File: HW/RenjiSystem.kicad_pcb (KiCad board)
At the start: 2 copper layers, 45 parts, among them J1 Conn_AE_LXDC55_3.3V, J10 Conn_Debug, J11 Conn_AE_QFP100PR5_DIP_51_75, J12 Conn_SwitchBoard, J13 Conn_LEDIndicator, J2 Conn_LCD, J3 Conn_AE_QFP100PR5_DIP_26_50, J4 Conn_AE_QFP100PR5_DIP_1_25, J5 Conn_AE_LXDC55_5V, J6 Conn_AE_QFP100PR5_DIP_76_100, J7 Conn_Ethernet, J8 Conn_UART1, J9 Conn_UART2, K1 G5Q-14_DC5, K2 G5Q-14_DC5, K3 G5Q-14_DC5, Q1 2SC1815, Q2 2SC1815, Q3 2SC1815, T1 Transformer_FS24-100-C2

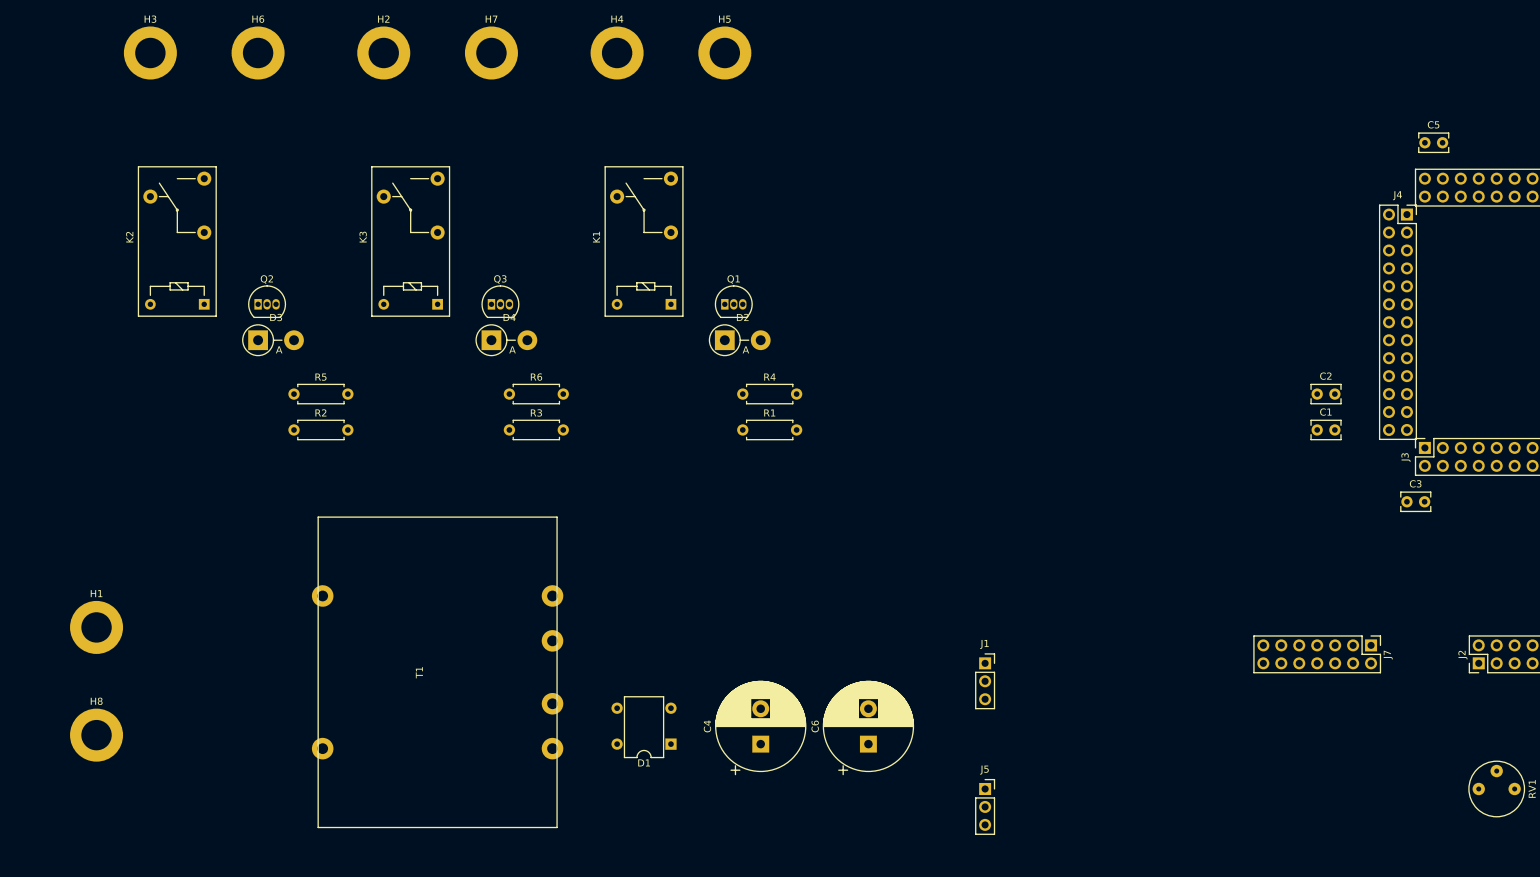
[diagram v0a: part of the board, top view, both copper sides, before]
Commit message: 電源部配線
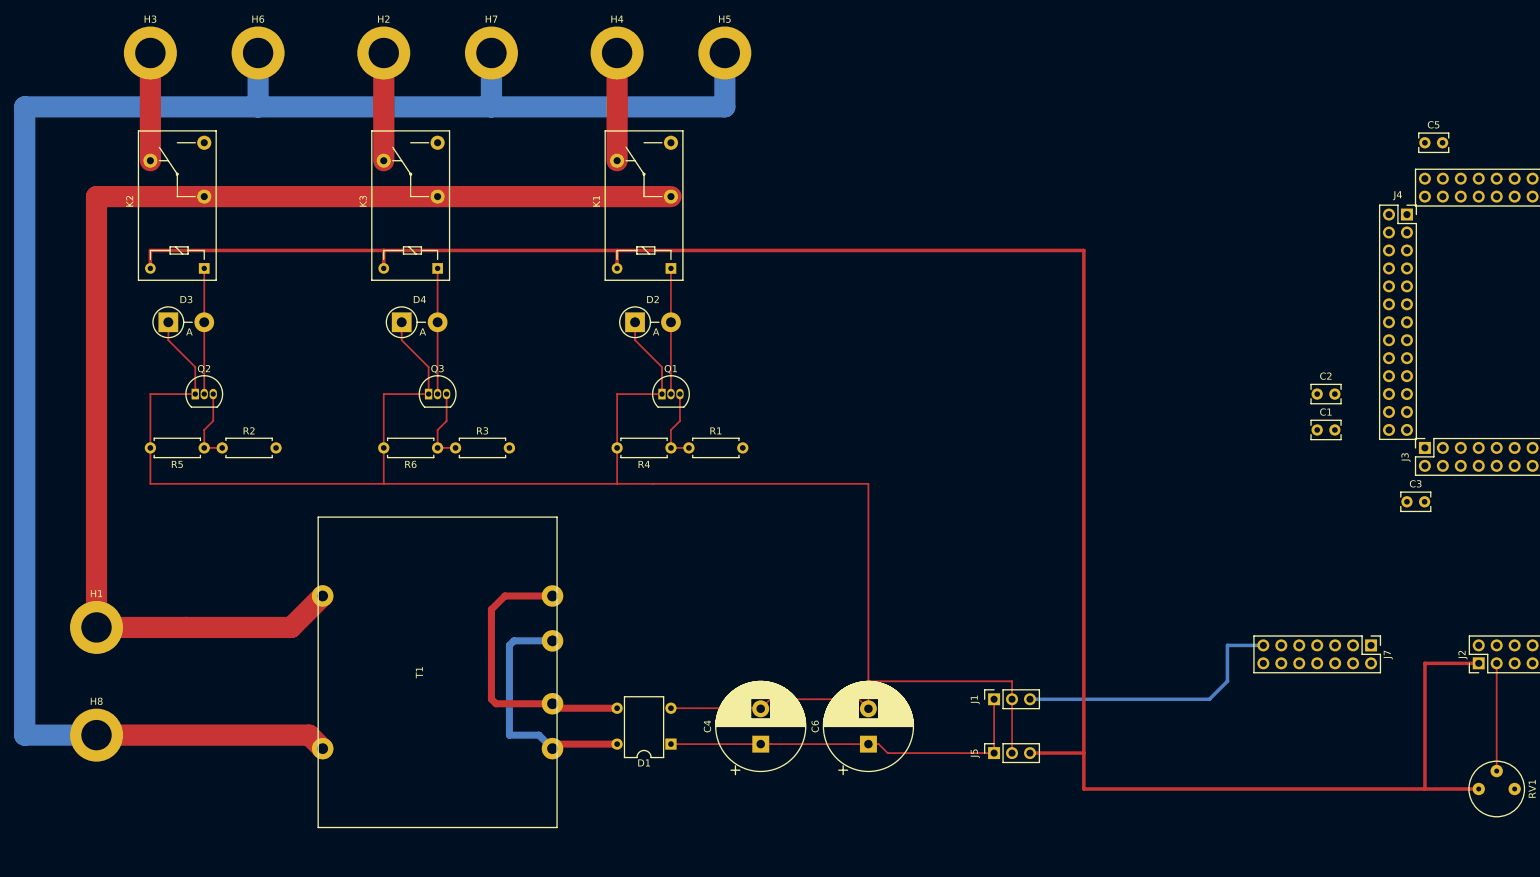
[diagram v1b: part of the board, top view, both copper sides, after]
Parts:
- moved Q1 15.5 mm to (105.4, 66.0)
- moved Q2 15.5 mm to (39.4, 66.0)
- moved Q3 15.5 mm to (72.4, 66.0)
- moved R5 14.8 mm to (40.6, 73.7), turned to 180 degrees
- moved D2 13.0 mm to (101.6, 55.9)
- moved D4 13.0 mm to (68.6, 55.9)
- moved D3 13.0 mm to (35.6, 55.9)
- moved R4 12.7 mm to (106.7, 73.7), turned to 180 degrees
- moved R6 12.7 mm to (73.7, 73.7), turned to 180 degrees
- moved R2 10.5 mm to (43.2, 73.7)
- moved R1 8.03 mm to (109.2, 73.7)
- moved R3 8.03 mm to (76.2, 73.7)
- moved J1 5.24 mm to (152.4, 109.2), turned to 90 degrees
- moved J5 5.24 mm to (152.4, 116.8), turned to 90 degrees
- moved K1 5.08 mm to (106.7, 48.3)
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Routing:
- net +5V: track 0.00 -> 304.8 mm
- net GND: track 0.00 -> 285.4 mm
- net Earth: track 0.00 -> 253.8 mm
- net POWER_IN_HOT: track 0.00 -> 176.1 mm
- net +9V: track 0.00 -> 53.9 mm
- net Net-(D1-Pad3): track 0.00 -> 40.4 mm
- net +3V3: track 0.00 -> 39.2 mm
- net Net-(D1-Pad4): track 0.00 -> 35.4 mm
- net Net-(D4-Pad2): track 0.00 -> 17.8 mm
- net Net-(D3-Pad2): track 0.00 -> 17.8 mm
- net Net-(D2-Pad2): track 0.00 -> 17.8 mm
- net Net-(H4-Pad1): track 0.00 -> 15.2 mm
- net Net-(H3-Pad1): track 0.00 -> 15.2 mm
- net Net-(H2-Pad1): track 0.00 -> 15.2 mm
- net CONTRAST_ADJ: track 0.00 -> 15.2 mm
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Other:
- net class AC100VLine added: clearance 10, trace_width 3, via_dia 1.5, via_drill 1.1
- net class AC12VLine added: clearance 3, trace_width 1, via_dia 0.8, via_drill 0.4
- net class DC3.3VPowerLine added: clearance 0.5, trace_width 0.5, via_dia 0.8, via_drill 0.4
- net class DC5VPowerLine added: clearance 0.5, trace_width 0.5, via_dia 0.8, via_drill 0.4
- net class DC9VPowerLine added: clearance 1, trace_width 0.8, via_dia 0.8, via_drill 0.4

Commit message: ボード回路図を, シート分割
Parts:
- moved J9 116.9 mm to (274.3, 16.5), turned to 0 degrees
- moved J8 102.3 mm to (274.3, 27.9), turned to 0 degrees
- moved J10 87.8 mm to (274.3, 39.4), turned to 0 degrees
- moved J12 70.1 mm to (191.8, 34.3)
- moved Q2 50.8 mm to (90.2, 66.0)
- moved R2 50.8 mm to (94.0, 73.7)
- moved D3 50.8 mm to (86.4, 55.9)
- moved R5 50.8 mm to (91.4, 73.7)
- moved C5 41.9 mm to (254.0, 40.6)
- moved H2 33.0 mm to (33.0, 17.8)
- moved H3 33.0 mm to (66.0, 17.8)
- moved H6 33.0 mm to (81.3, 17.8)
- moved H7 33.0 mm to (48.3, 17.8)
- moved K2 33.0 mm to (73.7, 48.3)
- moved K3 33.0 mm to (40.6, 48.3)
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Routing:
- net +3V3: track 39.2 -> 295.4 mm, vias 0 -> 2
- net GND: track 285.4 -> 36.9 mm, vias 0 -> 1
- net FAN_CONTROL_SIGNAL: track 0.00 -> 193.6 mm, vias 0 -> 1
- net HEATER_CONTROL_SIGNAL: track 0.00 -> 160.6 mm, vias 0 -> 1
- net UV_CONTROL_SIGNAL: track 0.00 -> 122.5 mm, vias 0 -> 1
- net +5V: track 304.8 -> 383.5 mm
- net NRST: track 0.00 -> 68.7 mm
- net ETH_TXD1: track 0.00 -> 65.8 mm
- net ETH_TXD0: track 0.00 -> 65.8 mm
- net ETH_MDC: track 0.00 -> 60.2 mm
- net UART2_TX: track 0.00 -> 56.2 mm
- net ETH_TX_EN: track 0.00 -> 51.4 mm
- net UART2_RX: track 0.00 -> 50.0 mm
- net ETH_RXD1: track 0.00 -> 39.9 mm
- net UART1_RX: track 0.00 -> 39.9 mm
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- added copper zone on B.Cu, net GND
- added copper zone on F.Cu, net GND
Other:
- net class AC100VLine: clearance 10 -> 1.3; trace_width 3 -> 2
- net class AC12VLine: clearance 3 -> 0.65
- net class DC3.3VPowerLine: clearance 0.5 -> 0.25; trace_width 0.5 -> 0.25
- net class DC5VPowerLine: clearance 0.5 -> 0.25
- net class DC9VPowerLine: clearance 1 -> 0.25

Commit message: Ethernetボードの配置のためにレイアウト変更
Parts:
- removed H7: MountingHole_Pad_FAN_COLD, MountingHole:MountingHole_4.3mm_M4_DIN965_Pad
- removed H8: MountingHole_Pad_AC100V_COLD, MountingHole:MountingHole_4.3mm_M4_DIN965_Pad
- added J14: Conn_AE_QFP100PR5_DIP_76_100, Connector_PinSocket_2.54mm:PinSocket_2x13_P2.54mm_Vertical, F.Cu at (233.7, 91.4)
- added J15: Conn_LCD, Connector_PinHeader_2.54mm:PinHeader_2x07_P2.54mm_Vertical, F.Cu at (194.3, 41.9)
- added J16: Conn_Ethernet, Connector_PinHeader_2.54mm:PinHeader_2x07_P2.54mm_Vertical, F.Cu at (160.0, 36.8)
- added J17: Conn_UART1, Connector_PinHeader_2.54mm:PinHeader_1x03_P2.54mm_Horizontal, F.Cu at (217.2, 130.8)
- added J18: Conn_UART2, Connector_PinHeader_2.54mm:PinHeader_1x03_P2.54mm_Horizontal, F.Cu at (205.7, 130.8)
- added J19: Conn_Debug, Connector_PinHeader_2.54mm:PinHeader_1x05_P2.54mm_Horizontal, F.Cu at (233.7, 130.8)
- added J20: Conn_SwitchBoard, Connector_PinSocket_2.54mm:PinSocket_1x08_P2.54mm_Vertical, F.Cu at (218.4, 41.9)
- added J21: Conn_LEDIndicator, Connector_PinSocket_2.54mm:PinSocket_1x06_P2.54mm_Vertical, F.Cu at (238.8, 41.9)
- C1: value 1uF -> CP1; footprint Capacitor_THT:C_Rect_L4.0mm_W2.5mm_P2.50mm -> Capacitor_THT:CP_Radial_D12.5mm_P5.00mm
- C2: value 10nF -> CP1; footprint Capacitor_THT:C_Rect_L4.0mm_W2.5mm_P2.50mm -> Capacitor_THT:CP_Radial_D12.5mm_P5.00mm
- C3: value 2.2uF -> 1uF
- C4: value CP1 -> 10nF; footprint Capacitor_THT:CP_Radial_D12.5mm_P5.00mm -> Capacitor_THT:C_Rect_L4.0mm_W2.5mm_P2.50mm
- C6: value CP1 -> 2.2uF; footprint Capacitor_THT:CP_Radial_D12.5mm_P5.00mm -> Capacitor_THT:C_Rect_L4.0mm_W2.5mm_P2.50mm
- H1: value MountingHole_Pad_AC100V_HOT -> MountingHole; footprint MountingHole:MountingHole_4.3mm_M4_DIN965_Pad -> MountingHole:MountingHole_3.2mm_M3
- H2: value MountingHole_Pad_FAN_HOT -> MountingHole; footprint MountingHole:MountingHole_4.3mm_M4_DIN965_Pad -> MountingHole:MountingHole_3.2mm_M3
- H3: value MountingHole_Pad_HEATER_HOT -> MountingHole; footprint MountingHole:MountingHole_4.3mm_M4_DIN965_Pad -> MountingHole:MountingHole_3.2mm_M3
- H4: value MountingHole_Pad_UV_HOT -> MountingHole; footprint MountingHole:MountingHole_4.3mm_M4_DIN965_Pad -> MountingHole:MountingHole_3.2mm_M3
- H5: value MountingHole_Pad_UV_COLD -> MountingHole; footprint MountingHole:MountingHole_4.3mm_M4_DIN965_Pad -> MountingHole:MountingHole_3.2mm_M3
- H6: value MountingHole_Pad_HEATER_COLD -> MountingHole; footprint MountingHole:MountingHole_4.3mm_M4_DIN965_Pad -> MountingHole:MountingHole_3.2mm_M3
- J1: value Conn_AE_LXDC55_3.3V -> Screw_Terminal_AC100VHOT; footprint Connector_PinSocket_2.54mm:PinSocket_1x03_P2.54mm_Vertical -> MyFootPrintLibrary:PCB-20(632)F
- J10: value Conn_Debug -> Conn_AE_LXDC55_5V; footprint Connector_PinHeader_2.54mm:PinHeader_1x05_P2.54mm_Horizontal -> Connector_PinSocket_2.54mm:PinSocket_1x03_P2.54mm_Vertical
- J11: value Conn_AE_QFP100PR5_DIP_51_75 -> Conn_AE_QFP100PR5_DIP_1_25
- J12: value Conn_SwitchBoard -> Conn_AE_QFP100PR5_DIP_26_50; footprint Connector_PinSocket_2.54mm:PinSocket_1x08_P2.54mm_Vertical -> Connector_PinSocket_2.54mm:PinSocket_2x13_P2.54mm_Vertical
- J13: value Conn_LEDIndicator -> Conn_AE_QFP100PR5_DIP_51_75; footprint Connector_PinSocket_2.54mm:PinSocket_1x06_P2.54mm_Vertical -> Connector_PinSocket_2.54mm:PinSocket_2x13_P2.54mm_Vertical
- J2: value Conn_LCD -> Screw_Terminal_AC100VCOLD; footprint Connector_PinHeader_2.54mm:PinHeader_2x07_P2.54mm_Vertical -> MyFootPrintLibrary:PCB-20(632)F
- J3: value Conn_AE_QFP100PR5_DIP_26_50 -> Screw_Terminal_UV_HOT; footprint Connector_PinSocket_2.54mm:PinSocket_2x13_P2.54mm_Vertical -> MyFootPrintLibrary:PCB-20(632)F
- J4: value Conn_AE_QFP100PR5_DIP_1_25 -> Screw_Terminal_UV_COLD; footprint Connector_PinSocket_2.54mm:PinSocket_2x13_P2.54mm_Vertical -> MyFootPrintLibrary:PCB-20(632)F
- J5: value Conn_AE_LXDC55_5V -> Screw_Terminal_HEATER_HOT; footprint Connector_PinSocket_2.54mm:PinSocket_1x03_P2.54mm_Vertical -> MyFootPrintLibrary:PCB-20(632)F
- J6: value Conn_AE_QFP100PR5_DIP_76_100 -> Screw_Terminal_HEATER_COLD; footprint Connector_PinSocket_2.54mm:PinSocket_2x13_P2.54mm_Vertical -> MyFootPrintLibrary:PCB-20(632)F
- J7: value Conn_Ethernet -> Screw_Terminal_FAN_HOT; footprint Connector_PinHeader_2.54mm:PinHeader_2x07_P2.54mm_Vertical -> MyFootPrintLibrary:PCB-20(632)F
- J8: value Conn_UART1 -> Screw_Terminal_FAN_COLD; footprint Connector_PinHeader_2.54mm:PinHeader_1x03_P2.54mm_Horizontal -> MyFootPrintLibrary:PCB-20(632)F
- J9: value Conn_UART2 -> Conn_AE_LXDC55_3.3V; footprint Connector_PinHeader_2.54mm:PinHeader_1x03_P2.54mm_Horizontal -> Connector_PinSocket_2.54mm:PinSocket_1x03_P2.54mm_Vertical
- R3: value 1k -> 10k
- R5: value 10k -> 1k
- moved H2 207.3 mm to (240.0, 29.2)
- moved H4 185.6 mm to (240.0, 138.4)
- moved J9 179.7 mm to (134.6, 129.5), turned to 90 degrees
- moved J2 169.7 mm to (52.1, 120.7), turned to 180 degrees
- moved H6 156.5 mm to (185.4, 134.6)
- moved J10 151.9 mm to (134.6, 99.1), turned to 90 degrees
- moved J4 148.4 mm to (62.5, 38.2), turned to 90 degrees
- moved J6 148.3 mm to (95.5, 38.1)
- moved J8 146.1 mm to (128.5, 38.2), turned to 270 degrees
- moved J3 139.5 mm to (78.5, 38.2)
- moved H5 126.9 mm to (163.8, 134.6)
- moved H3 123.0 mm to (41.9, 138.4)
- moved J1 101.1 mm to (51.6, 100.5), turned to 180 degrees
- moved C4 99.6 mm to (205.7, 66.0), turned to 180 degrees
- moved C6 97.4 mm to (228.6, 90.2), turned to 180 degrees
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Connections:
- C1 pad 1: GND -> /Power/Rectified_DC9V
- C1 pad 2: +3V3 -> GND
- C2 pad 1: +3V3 -> /Power/Rectified_DC9V
- C3 pad 1: Net-(C3-Pad1) -> GND
- C3 pad 2: GND -> +BATT
- C4 pad 1: +9V -> +BATT
- C5 pad 1: Net-(C5-Pad1) -> /MCU/VCAP1
- C6 pad 1: +9V -> /MCU/VCAP2
- D1 pad 1: +9V -> /Power/Rectified_DC9V
- H1 pad 1: POWER_IN_HOT -> (no net)
- H2 pad 1: Net-(H2-Pad1) -> (no net)
- H3 pad 1: Net-(H3-Pad1) -> (no net)
- H4 pad 1: Net-(H4-Pad1) -> (no net)
- H5 pad 1: Earth -> (no net)
- H6 pad 1: Earth -> (no net)
- J1 pad 1: +9V -> /Instruments/AC100V_HOT
- J10 pad 1: +3V3 -> /Power/Rectified_DC9V
- J10 pad 2: SYS_SWCLK -> GND
- J10 pad 3: GND -> /Instruments/CTRL_POWER_IN
- J11 pad 1: ETH_TXD0 -> /MCU/SETTING_BUTTON_UP
- J11 pad 10: Net-(J11-Pad10) -> GND
- J11 pad 11: UV_CONTROL_SIGNAL -> +BATT
- J11 pad 12: HEATER_CONTROL_SIGNAL -> (no net)
- J11 pad 13: FAN_CONTROL_SIGNAL -> (no net)
- J11 pad 14: Net-(J11-Pad14) -> /Debug/DBG2
- J11 pad 15: Net-(J11-Pad15) -> (no net)
- J11 pad 16: Net-(J11-Pad16) -> /Ethernet/ETHER_CTRL8
- J11 pad 17: Net-(J11-Pad17) -> (no net)
- J11 pad 18: UART1_TX -> (no net)
- J11 pad 19: UART1_RX -> +BATT
- J11 pad 2: ETH_TXD1 -> /MCU/SETTING_BUTTON_SELECT
- J11 pad 20: Net-(J11-Pad20) -> GND
- J11 pad 21: Net-(J11-Pad21) -> +BATT
- J11 pad 22: SYS_SWDIO -> +BATT
- J11 pad 23: Net-(C5-Pad1) -> (no net)
- J11 pad 24: GND -> /Ethernet/ETHER_CTRL3
- J11 pad 25: +3V3 -> /Ethernet/ETHER_CTRL4
- J11 pad 26: Net-(J11-Pad26) -> (no net)
- J11 pad 3: LED_SIGNAL_RED -> /MCU/SETTING_BUTTON_DOWN
- J11 pad 4: LED_SIGNAL_GREEN -> /MCU/SWITCH_SIGNAL3
- J11 pad 5: LED_SIGNAL_ORANGE -> /MCU/SWITCH_SIGNAL4
- J11 pad 6: LED_SIGNAL_GREEN2 -> +BATT
- J11 pad 7: Net-(J11-Pad7) -> /MCU/RESERVED_SWITCH1
- J11 pad 8: Net-(J11-Pad8) -> /MCU/RESERVED_SWITCH2
- J11 pad 9: Net-(J11-Pad9) -> (no net)
- J12 pad 1: SETTING_BUTTON_UP -> (no net)
- J12 pad 2: SETTING_BUTTON_SELECT -> GND
- J12 pad 3: SETTING_BUTTON_DOWN -> +BATT
- J12 pad 4: UV_CONTROL_SWTICH -> (no net)
- J12 pad 5: TEMP_SETTING_SWITCH -> (no net)
- J12 pad 6: RESERVED_SWITCH1 -> (no net)
- J12 pad 7: RESERVED_SWITCH2 -> /Ethernet/ETHER_CTRL7
- J12 pad 8: GND -> /Ethernet/ETHER_CTRL2
- J13 pad 1: +5V -> /Ethernet/ETHER_CTRL5
- J13 pad 2: LED_SIGNAL_RED -> /Ethernet/ETHER_CTRL0
- J13 pad 3: LED_SIGNAL_GREEN -> (no net)
- J13 pad 4: LED_SIGNAL_ORANGE -> (no net)
- J13 pad 5: LED_SIGNAL_GREEN2 -> (no net)
- J13 pad 6: GND -> (no net)
- J2 pad 1: +5V -> Earth
- J3 pad 1: Net-(J3-Pad1) -> /Instruments/UV_DRIVE_HOT
- J4 pad 1: SETTING_BUTTON_UP -> Earth
- J5 pad 1: +9V -> /Instruments/HEATER_DRIVE_HOT
- J6 pad 1: SYS_SWCLK -> Earth
- J7 pad 1: ETH_TXD1 -> /Instruments/FAN_DRIVE_HOT
- J8 pad 1: UART1_TX -> Earth
- J9 pad 1: UART2_TX -> /Power/Rectified_DC9V
- J9 pad 2: UART2_RX -> GND
- J9 pad 3: GND -> +BATT
- K1 pad 2: POWER_IN_HOT -> /Instruments/AC100V_HOT
- K1 pad 3: Net-(K1-Pad3) -> /Instruments/UV_DRIVE_HOT
- K1 pad 4: Net-(H4-Pad1) -> (no net)
- K1 pad 5: +5V -> /Instruments/CTRL_POWER_IN
- K2 pad 2: POWER_IN_HOT -> /Instruments/AC100V_HOT
- K2 pad 3: Net-(K2-Pad3) -> /Instruments/FAN_DRIVE_HOT
- K2 pad 4: Net-(H3-Pad1) -> (no net)
- K2 pad 5: +5V -> /Instruments/CTRL_POWER_IN
- K3 pad 2: POWER_IN_HOT -> /Instruments/AC100V_HOT
- K3 pad 3: Net-(K3-Pad3) -> /Instruments/HEATER_DRIVE_HOT
- K3 pad 4: Net-(H2-Pad1) -> (no net)
- K3 pad 5: +5V -> /Instruments/CTRL_POWER_IN
- R1 pad 2: UV_CONTROL_SIGNAL -> /MCU/HEATER_CONTROL_SIGNAL
- R2 pad 2: HEATER_CONTROL_SIGNAL -> /Instruments/FAN_CONTROL_SIGNAL
- R3 pad 1: Net-(Q3-Pad3) -> Net-(Q1-Pad3)
- R3 pad 2: FAN_CONTROL_SIGNAL -> GND
- R4 pad 1: Net-(Q1-Pad3) -> Net-(Q2-Pad3)
- R5 pad 1: Net-(Q2-Pad3) -> Net-(Q3-Pad3)
- R5 pad 2: GND -> /Instruments/HEATER_CONTROL_SIGNAL
- RV1 pad 1: +5V -> /Instruments/CTRL_POWER_IN
- RV1 pad 2: CONTRAST_ADJ -> /LCD/CONTRAST_ADJ
- T1 pad 1: POWER_IN_HOT -> /Instruments/AC100V_HOT
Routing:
- net +5V: track 383.5 -> 0.00 mm
- net +BATT: track 0.00 -> 346.2 mm
- net /Instruments/CTRL_POWER_IN: track 0.00 -> 296.5 mm
- net +3V3: track 295.4 -> 0.00 mm, vias 2 -> 0
- net FAN_CONTROL_SIGNAL: track 193.6 -> 0.00 mm, vias 1 -> 0
- net POWER_IN_HOT: track 176.1 -> 0.00 mm
- net /MCU/HEATER_CONTROL_SIGNAL: track 0.00 -> 171.4 mm
- net HEATER_CONTROL_SIGNAL: track 160.6 -> 0.00 mm, vias 1 -> 0
- net /Instruments/AC100V_HOT: track 0.00 -> 158.2 mm
- net /Instruments/HEATER_CONTROL_SIGNAL: track 0.00 -> 137.6 mm
- net UV_CONTROL_SIGNAL: track 122.5 -> 0.00 mm, vias 1 -> 0
- net /Instruments/FAN_CONTROL_SIGNAL: track 0.00 -> 104.6 mm
- net /Debug/UART21: track 0.00 -> 102.9 mm
- net /Ethernet/ETHER_CTRL5: track 0.00 -> 101.3 mm
- net /Ethernet/ETHER_CTRL0: track 0.00 -> 100.4 mm
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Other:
- board outline added: 205.7 x 116.8 mm
- net class AC100VLine: via_dia 1.5 -> 3.3; via_drill 1.1 -> 1.3
- net class AC12VLine removed
- net class DC3.3VPowerLine removed
- net class DC5VPowerLine removed
- net class DC9VPowerLine removed
- net class Default: trace_width 0.25 -> 0.4; via_dia 0.8 -> 1
- rule pad_to_mask_clearance: 0.051 -> 0
- board text added: "AE_LXDC55-3.3V"
- board text added: "AE_LXDC55-5V"
- board text added: "Ethernet"
- board text added: "LAN8720A board"
- board text added: "LCD"
- board text added: "LED board"
- board text added: "Switch board"

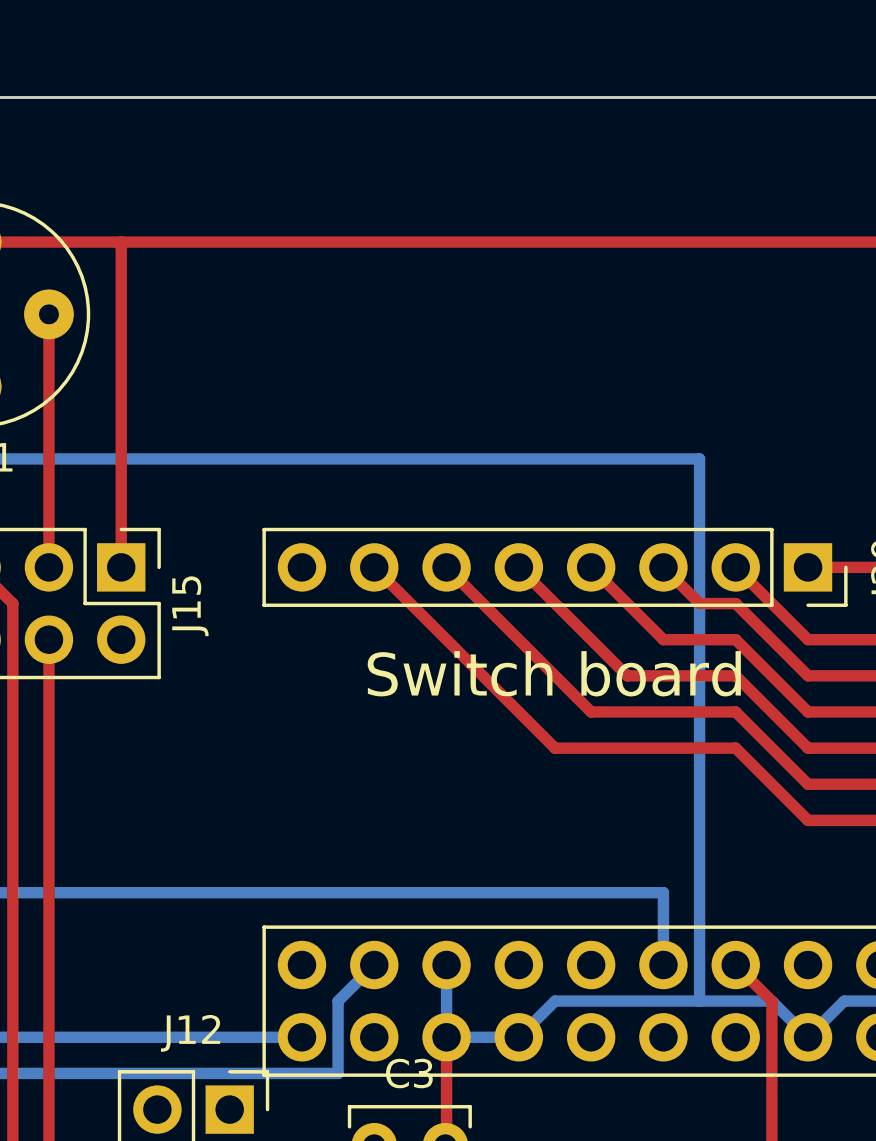
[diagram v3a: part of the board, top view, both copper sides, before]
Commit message: サーミスタの端子を追記
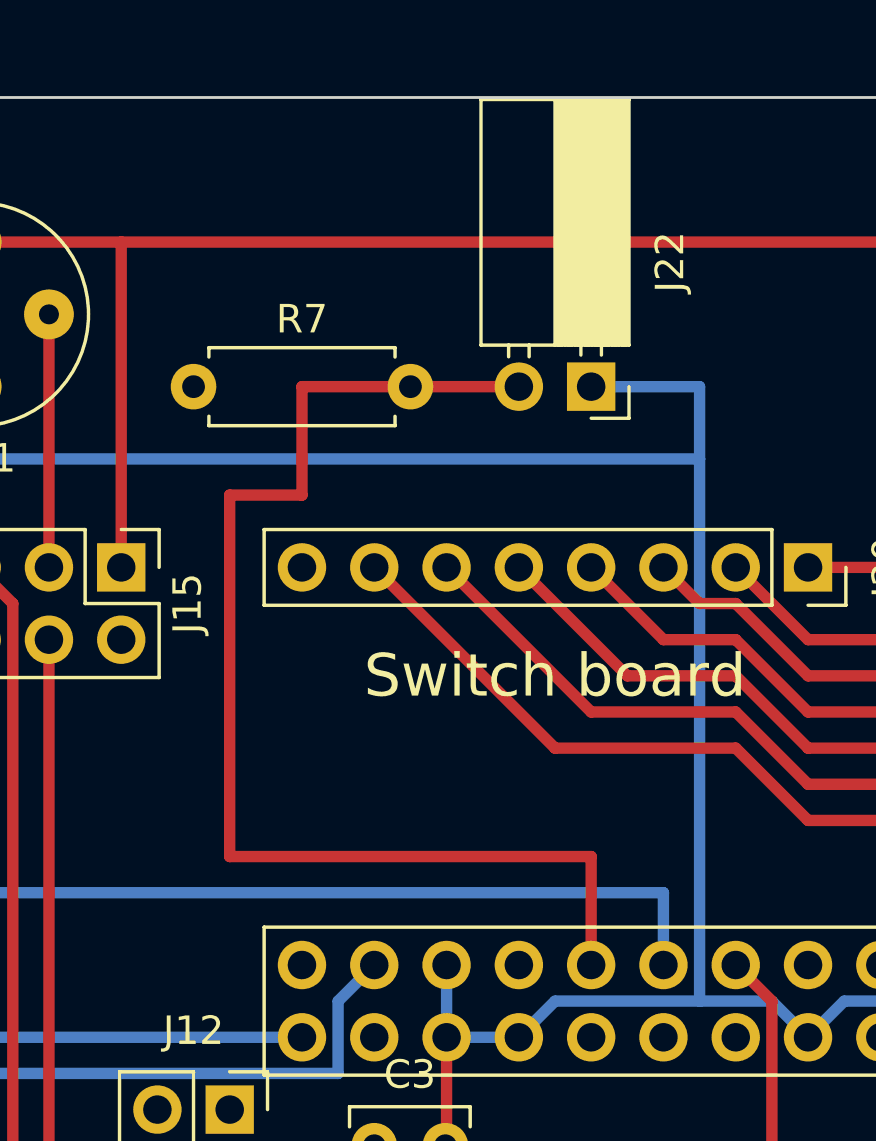
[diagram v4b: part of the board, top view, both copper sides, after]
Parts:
- added J22: Conn_Thermistor, Connector_PinSocket_2.54mm:PinSocket_1x02_P2.54mm_Horizontal, F.Cu at (210.8, 35.6)
- added R7: 10k, Resistor_THT:R_Axial_DIN0207_L6.3mm_D2.5mm_P7.62mm_Horizontal, F.Cu at (196.8, 35.6)
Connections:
- J11 pad 18: (no net) -> /MCU/ThermistorIn
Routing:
- net /MCU/ThermistorIn: track 0.00 -> 43.2 mm
- net +BATT: track 346.2 -> 352.6 mm
